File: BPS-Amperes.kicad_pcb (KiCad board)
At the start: 2 copper layers, 40 x 50 mm, 35 parts, among them J1 Conn_02x10_Odd_Even, J2 ShuntConn, J3 PassthroughConn, J4 TestConn, J5 Conn_01x02, U1 INA186A3IDDFT, U2 OPA2196, U4 REF1930AIDDCT

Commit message: Flipped components to the back
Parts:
- C1, C10, C11, C12, C13, C2, C3, C4, C5, C6, C7, C9, D1, D2, FB1, FB2, LOGO0, LOGO1, R1, R2, R3, R4, R5, R6, U1, U2, U4: moved to B.Cu
- moved LOGO1 33.3 mm to (161.5, 111.5), turned to 180 degrees
- moved LOGO0 13.6 mm to (149.9, 80.8), turned to 180 degrees
- moved C13 9.55 mm to (148.0, 91.8), turned to 90 degrees
- moved R6 7.07 mm to (131.5, 81.5), turned to 90 degrees
- moved C11 5.79 mm to (140.1, 95.5)
- moved C12 5.79 mm to (140.1, 98.0)
- moved FB2 5.79 mm to (140.1, 93.0)
- moved C9 5.65 mm to (144.5, 97.5)
- moved C10 5.65 mm to (144.5, 100.0)
- moved FB1 5.65 mm to (144.5, 95.0)
- moved C1 5.18 mm to (140.0, 100.5)
- moved D2 5.03 mm to (131.5, 78.0), turned to -90 degrees
- moved U4 4.98 mm to (144.6, 91.7), turned to -90 degrees
- moved J5 1.13 mm to (139.5, 76.2)
- moved U1 1.08 mm to (145.2, 103.9)
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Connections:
- J5 pad 1: +3V0 -> +1V5
- J5 pad 2: +1V5 -> +3V0

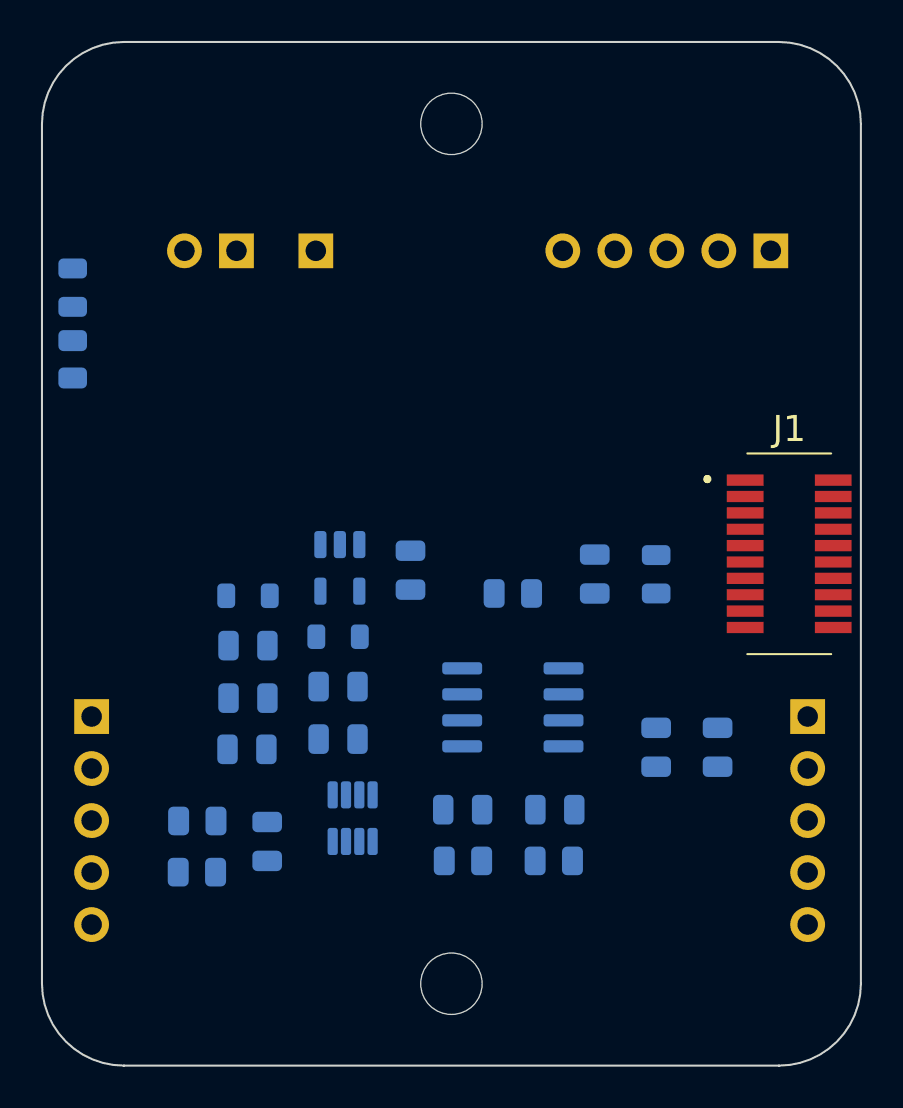
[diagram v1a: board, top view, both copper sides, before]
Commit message: adding ground plane to the back
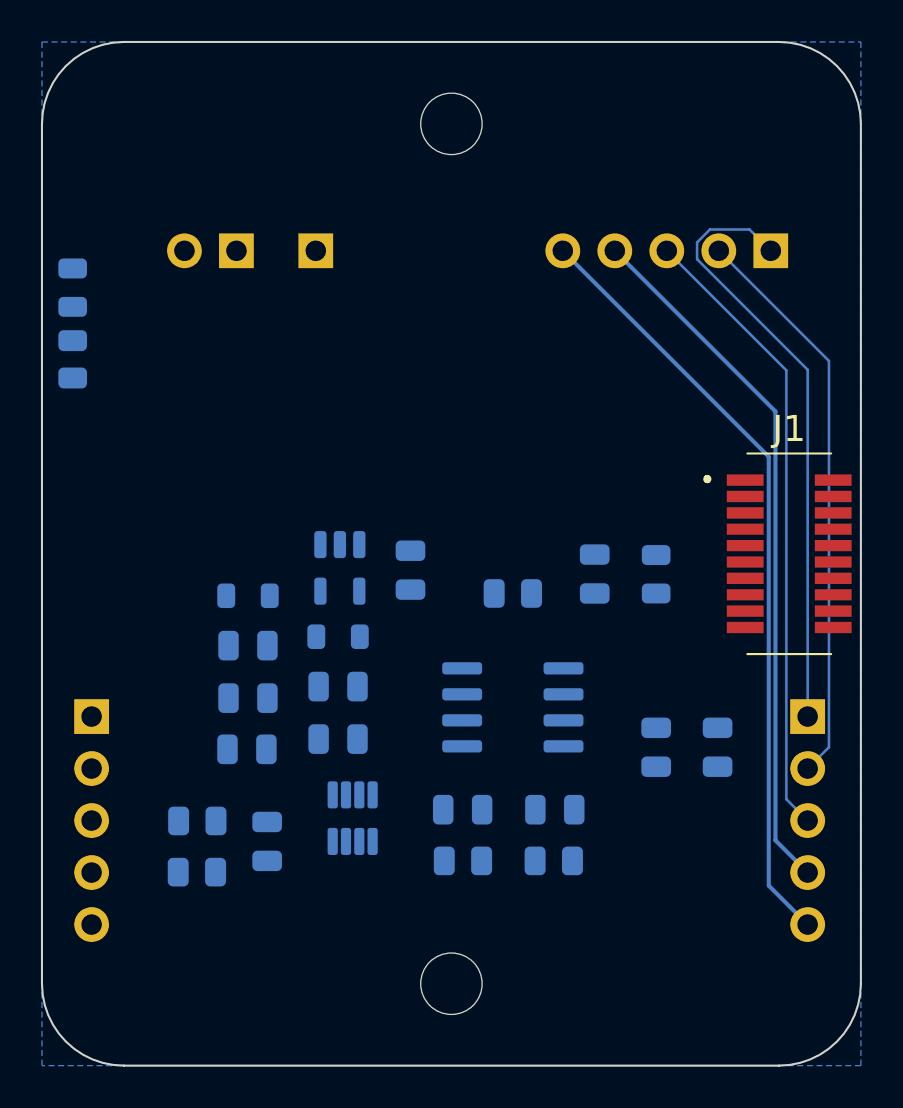
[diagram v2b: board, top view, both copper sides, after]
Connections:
- net Net-(J3-Pin_1) renamed /NOTCON
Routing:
- net /V-: track 0.00 -> 37.9 mm
- net /V+: track 0.00 -> 34.3 mm
- net /TEST: track 0.00 -> 30.7 mm
- net /NOTCON: track 0.00 -> 29.7 mm
- net /SHUNT: track 0.00 -> 27.9 mm
- added copper zone on B.Cu, net GND
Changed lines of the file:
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@@
   (net 32 "Net-(U2B--)")
   (net 33 "unconnected-(U1-NC-Pad6)")
-  (net 34 "Net-(J3-Pin_1)")
+  (net 34 "/NOTCON")
   (net 35 "/SHUNT")
   (net 36 "/TEST")
@@
     (pad "20" smd rect locked (at -3.6 2.15 90) (size 0.55 1.8) (layers "F.Cu" "F.Paste" "F.Mask")
       (net 18 "/Aout") (pinfunction "Pin_20") (pintype "passive"))
-    (model "${KIPRJMOD}/UTSVT-KiCadLibraries/utsvt3d/connectors.3dshapes/53307-2071.stp"
+    (model "${KIPRJMOD}/common/utsvt3d/connectors.3dshapes/53307-2071.stp"
       (offset (xyz 0 0 1.849999996))
       (scale (xyz 1 1 1))
@@
       (stroke (width 0.1) (type solid)) (layer "B.Fab"))
     (pad "1" thru_hole rect (at 0 0 90) (size 1.7 1.7) (drill 1) (layers "*.Cu" "*.Mask")
-      (net 34 "Net-(J3-Pin_1)") (pinfunction "Pin_1") (pintype "passive"))
+      (net 34 "/NOTCON") (pinfunction "Pin_1") (pintype "passive"))
     (pad "2" thru_hole oval (at 0 -2.54 90) (size 1.7 1.7) (drill 1) (layers "*.Cu" "*.Mask")
       (net 35 "/SHUNT") (pinfunction "Pin_2") (pintype "passive"))
@@
       (stroke (width 0.1) (type solid)) (layer "B.Fab"))
     (pad "1" thru_hole rect (at 0 0 180) (size 1.7 1.7) (drill 1) (layers "*.Cu" "*.Mask")
-      (net 34 "Net-(J3-Pin_1)") (pinfunction "Pin_1") (pintype "passive"))
+      (net 34 "/NOTCON") (pinfunction "Pin_1") (pintype "passive"))
     (pad "2" thru_hole oval (at 0 -2.54 180) (size 1.7 1.7) (drill 1) (layers "*.Cu" "*.Mask")
       (net 35 "/SHUNT") (pinfunction "Pin_2") (pintype "passive"))
@@
     (effects (font (size 1 1) (thickness 0.15)) (justify left bottom mirror))
   )
-  (gr_text "V-" (at 165.7 77.5 90) (layer "B.SilkS")
+  (gr_text "V-" (at 155.5 78 90) (layer "B.SilkS")
     (effects (font (size 1 1) (thickness 0.15)) (justify left bottom mirror))
   )
@@
     (effects (font (size 1 1) (thickness 0.15)) (justify left bottom))
   )
-  (gr_text "NC" (at 155.65 77.6 90) (layer "B.SilkS")
+  (gr_text "NC" (at 166.235 78 90) (layer "B.SilkS")
     (effects (font (size 1 1) (thickness 0.15)) (justify left bottom mirror))
   )
@@
     (effects (font (size 1 1) (thickness 0.15) bold) (justify mirror))
   )
-  (gr_text "SHUNT" (at 158.15 77.3 90) (layer "B.SilkS")
+  (gr_text "SHUNT" (at 163.5 78 90) (layer "B.SilkS")
     (effects (font (size 1 1) (thickness 0.15)) (justify left bottom mirror))
   )
@@
     (effects (font (size 1 1) (thickness 0.15) bold) (justify mirror))
   )
-  (gr_text "TEST" (at 160.7 77.3 90) (layer "B.SilkS")
+  (gr_text "TEST" (at 161 78 90) (layer "B.SilkS")
     (effects (font (size 1 1) (thickness 0.15)) (justify left bottom mirror))
   )
@@
     (effects (font (size 1 1) (thickness 0.15) bold) (justify mirror))
   )
-  (gr_text "V+" (at 163.2 77.6 90) (layer "B.SilkS")
+  (gr_text "V+" (at 158.5 78 90) (layer "B.SilkS")
     (effects (font (size 1 1) (thickness 0.15)) (justify left bottom mirror))
   )
@@
     (style (thickness 0.1) (arrow_length 1.27) (text_position_mode 0) (extension_height 0.58642) (extension_offset 0.5) keep_text_aligned)
   )
+  (segment (start 164.5595 75.1595) (end 165.6 76.2) (width 0.127) (layer "B.Cu") (net 34))
+  (segment (start 162 76.61149) (end 162 75.78851) (width 0.127) (layer "B.Cu") (net 34))
+  (segment (start 167.4 98.95) (end 167.4 82.01149) (width 0.127) (layer "B.Cu") (net 34))
+  (segment (start 162 75.78851) (end 162.62901 75.1595) (width 0.127) (layer "B.Cu") (net 34))
+  (segment (start 167.4 82.01149) (end 162 76.61149) (width 0.127) (layer "B.Cu") (net 34))
+  (segment (start 162.62901 75.1595) (end 164.5595 75.1595) (width 0.127) (layer "B.Cu") (net 34))
+  (segment (start 168.4405 100.4495) (end 167.4 101.49) (width 0.127) (layer "B.Cu") (net 35))
+  (segment (start 163.06 76.2) (end 168.4405 81.5805) (width 0.127) (layer "B.Cu") (net 35))
+  (segment (start 168.4405 81.5805) (end 168.4405 100.4495) (width 0.127) (layer "B.Cu") (net 35))
+  (segment (start 167.4 104.03) (end 166.3595 102.9895) (width 0.127) (layer "B.Cu") (net 36))
+  (segment (start 166.3595 102.9895) (end 166.3595 82.0395) (width 0.127) (layer "B.Cu") (net 36))
+  (segment (start 166.3595 82.0395) (end 160.52 76.2) (width 0.127) (layer "B.Cu") (net 36))
+  (segment (start 165.827 84.047) (end 157.98 76.2) (width 0.2) (layer "B.Cu") (net 37))
+  (segment (start 165.827 104.997) (end 165.827 84.047) (width 0.2) (layer "B.Cu") (net 37))
+  (segment (start 167.4 106.57) (end 165.827 104.997) (width 0.2) (layer "B.Cu") (net 37))
+  (segment (start 167.4 109.11) (end 165.5 107.21) (width 0.2) (layer "B.Cu") (net 38))
+  (segment (start 165.5 86.26) (end 155.44 76.2) (width 0.2) (layer "B.Cu") (net 38))
+  (segment (start 165.5 107.21) (end 165.5 86.26) (width 0.2) (layer "B.Cu") (net 38))
+  (zone (net 0) (net_name "") (layer "B.Cu") (hatch edge 0.5)
+    (connect_pads (clearance 0))
+    (min_thickness 0.5) (filled_areas_thickness no)
+    (keepout (tracks allowed) (vias allowed) (pads allowed) (copperpour not_allowed) (footprints allowed))
+    (fill (thermal_gap 0.5) (thermal_bridge_width 0.5))
+    (polygon
+      (pts
+        (xy 150.574997 95.810776)
+        (xy 155.166486 95.823185)
+        (xy 154.980345 101.159241)
+        (xy 150.612225 101.122012)
+      )
+    )
+  )
+  (zone (net 4) (net_name "GND") (layer "B.Cu") (hatch edge 0.5)
+    (connect_pads (clearance 0.5))
+    (min_thickness 0.5) (filled_areas_thickness no)
+    (fill yes (thermal_gap 0.5) (thermal_bridge_width 0.5))
+    (polygon
+      (pts
+        (xy 130 66)
+        (xy 170 66)
+        (xy 170 116)
+        (xy 130 116)
+      )
+    )
+  )
   (group "" (id 9c716276-2a82-4619-908a-de798b1d9a88)

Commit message: Initial tracing with no thoughts
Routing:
- net +3.3V: track 0.00 -> 73.5 mm, vias 0 -> 1
- net +3V0: track 0.00 -> 68.4 mm, vias 0 -> 1
- net GND: track 0.00 -> 49.1 mm, vias 0 -> 1
- net /Aout: track 0.00 -> 41.1 mm, vias 0 -> 2
- net +1V5: track 0.00 -> 34.9 mm, vias 0 -> 1
- net Net-(U2A--): track 0.00 -> 10.8 mm
- net Net-(U2A-+): track 0.00 -> 8.29 mm
- net Net-(U2B--): track 0.00 -> 7.92 mm
- net /RSHH: track 0.00 -> 7.03 mm
- net /RSHL: track 0.00 -> 6.34 mm
- net Net-(J2-Pin_2): track 0.00 -> 5.31 mm
- net /NOTCON: track 29.7 -> 24.5 mm
- net Net-(C3-Pad1): track 0.00 -> 5.12 mm
- net Net-(U4-VBIAS): track 0.00 -> 4.99 mm
- net Net-(U1-OUT): track 0.00 -> 3.89 mm
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
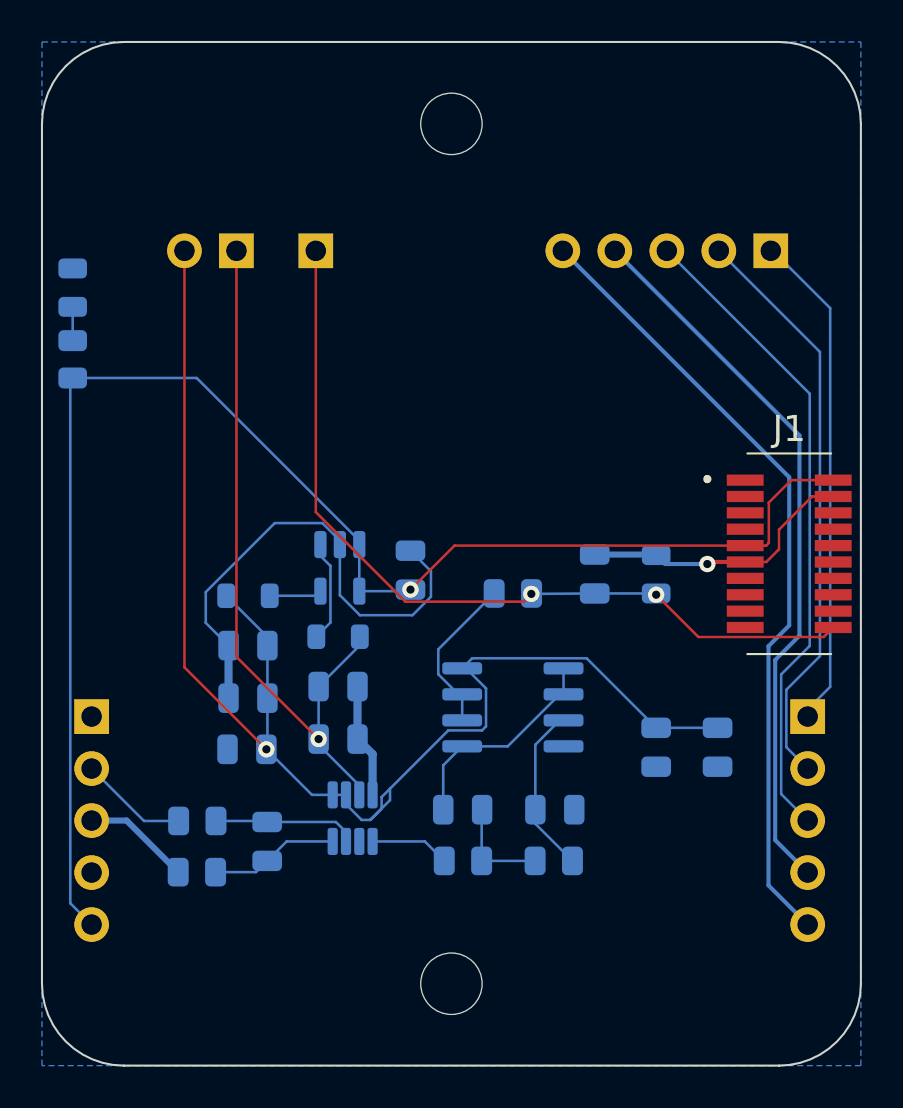
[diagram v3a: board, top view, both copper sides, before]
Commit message: Updated component blocking
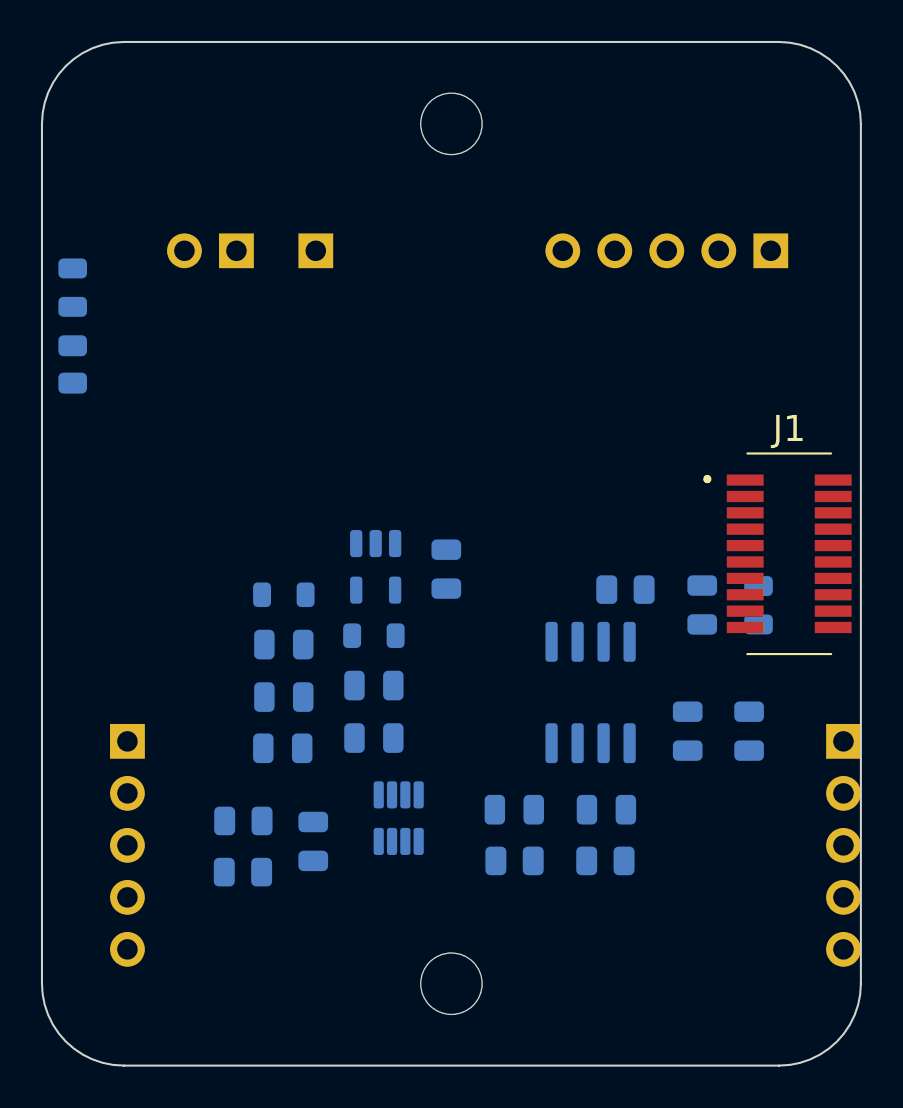
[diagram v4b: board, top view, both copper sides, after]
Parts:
- moved R5 5.50 mm to (158.5, 92.8)
- moved C6 5.46 mm to (162.2, 93.5)
- moved D1 5.22 mm to (165.0, 93.5)
- moved U2 3.87 mm to (156.8, 97.8), turned to 90 degrees
- moved R3 2.52 mm to (153.1, 106.0)
- moved R4 2.52 mm to (157.5, 106.0)
- moved C3 2.52 mm to (153.1, 103.5)
- moved C4 2.52 mm to (157.6, 103.5), turned to 180 degrees
- moved C2 2.25 mm to (143.2, 105.0)
- moved R1 2.25 mm to (139.8, 104.0)
- moved R2 2.25 mm to (139.8, 106.5)
- moved U1 2.25 mm to (147.4, 103.9)
- moved J2 2.13 mm to (134.2, 100.2)
- moved J3 2.13 mm to (169.2, 100.2)
- moved C1 1.75 mm to (141.8, 100.5)
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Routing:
- net +3.3V: track 73.5 -> 0.00 mm, vias 1 -> 0
- net +3V0: track 68.4 -> 0.00 mm, vias 1 -> 0
- net GND: track 49.1 -> 0.00 mm, vias 1 -> 0
- net /Aout: track 41.1 -> 0.00 mm, vias 2 -> 0
- net /V-: track 38.7 -> 0.00 mm
- net /V+: track 35.3 -> 0.00 mm
- net +1V5: track 34.9 -> 0.00 mm, vias 1 -> 0
- net /TEST: track 31.8 -> 0.00 mm
- net /SHUNT: track 28.4 -> 0.00 mm
- net /NOTCON: track 24.5 -> 0.00 mm
- net Net-(U2A--): track 10.8 -> 0.00 mm
- net Net-(U2A-+): track 8.29 -> 0.00 mm
- net Net-(U2B--): track 7.92 -> 0.00 mm
- net /RSHH: track 7.03 -> 0.00 mm
- net /RSHL: track 6.34 -> 0.00 mm
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- removed copper zone on B.Cu, net GND

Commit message: Fixed 3.3V Zener & Read Me
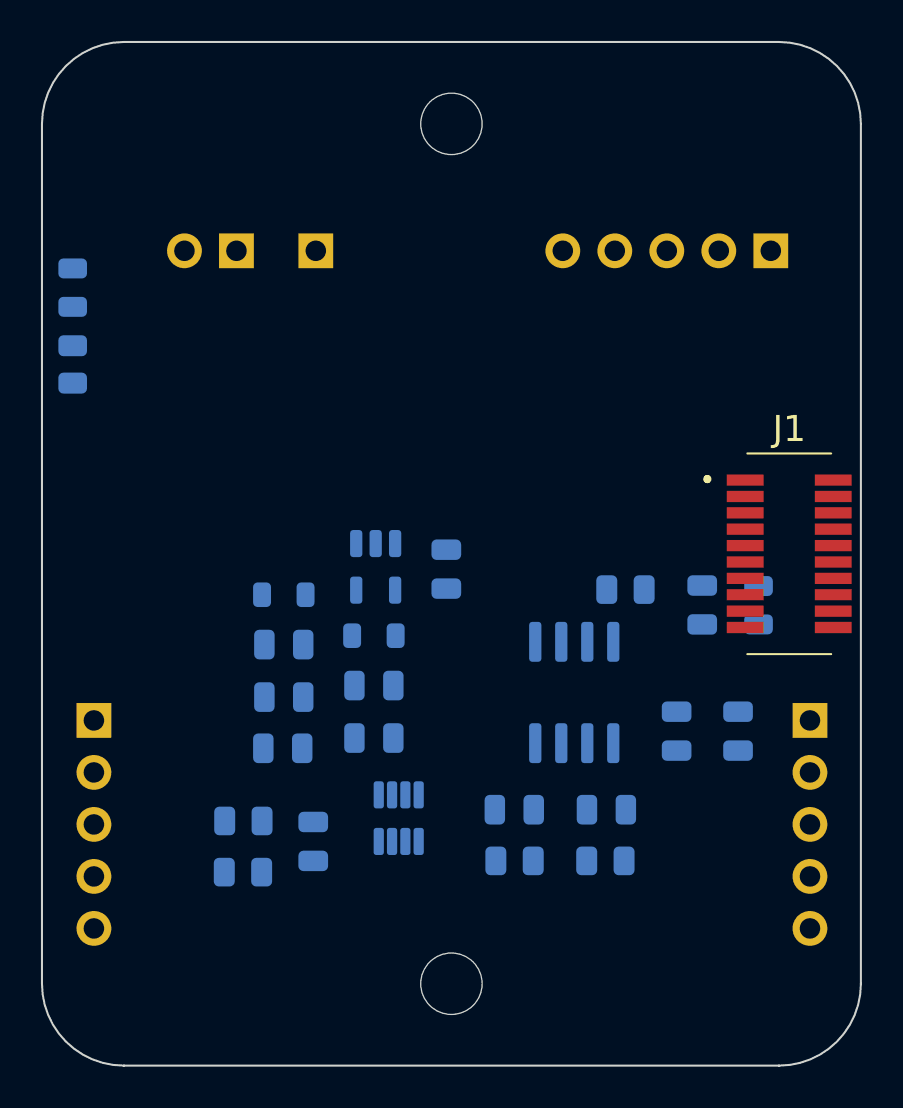
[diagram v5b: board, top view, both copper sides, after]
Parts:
- moved J2 1.93 mm to (132.5, 99.1)
- moved J3 1.93 mm to (167.5, 99.1)
- moved U2 0.80 mm to (156.0, 97.8)
- moved C5 0.54 mm to (164.0, 99.7)
- moved C7 0.54 mm to (161.0, 99.7)
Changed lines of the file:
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@@
   )
   (footprint "Capacitor_SMD:C_0805_2012Metric" (layer "B.Cu")
-    (at 164.54 99.6625 -90)
+    (at 164 99.6625 -90)
     (descr "Capacitor SMD 0805 (2012 Metric), square (rectangular) end terminal, IPC_7351 nominal, (Body size source: IPC-SM-782 page 76, https://www.pcb-3d.com/wordpress/wp-content/uploads/ipc-sm-782a_amendment_1_and_2.pdf, https://docs.google.com/spreadsheets/d/1BsfQQcO9C6DZCsRaXUlFlo91Tg2WpOkGARC1WS5S8t0/edit?usp=sharing), generated with kicad-footprint-generator")
     (tags "capacitor")
@@
   )
   (footprint "Connector_PinSocket_2.54mm:PinSocket_1x05_P2.54mm_Vertical" (layer "B.Cu")
-    (at 134.175 100.1625 180)
+    (at 132.537179 99.138763 180)
     (descr "Through hole straight socket strip, 1x05, 2.54mm pitch, single row (from Kicad 4.0.7), script generated")
     (tags "Through hole socket strip THT 1x05 2.54mm single row")
@@
   )
   (footprint "Capacitor_SMD:C_0805_2012Metric" (layer "B.Cu")
-    (at 161.54 99.6625 -90)
+    (at 161 99.6625 -90)
     (descr "Capacitor SMD 0805 (2012 Metric), square (rectangular) end terminal, IPC_7351 nominal, (Body size source: IPC-SM-782 page 76, https://www.pcb-3d.com/wordpress/wp-content/uploads/ipc-sm-782a_amendment_1_and_2.pdf, https://docs.google.com/spreadsheets/d/1BsfQQcO9C6DZCsRaXUlFlo91Tg2WpOkGARC1WS5S8t0/edit?usp=sharing), generated with kicad-footprint-generator")
     (tags "capacitor")
@@
   )
   (footprint "Package_SO:SOIC-8_3.9x4.9mm_P1.27mm" (layer "B.Cu")
-    (at 156.7975 97.775 90)
+    (at 156 97.775 90)
     (descr "SOIC, 8 Pin (JEDEC MS-012AA, https://www.analog.com/media/en/package-pcb-resources/package/pkg_pdf/soic_narrow-r/r_8.pdf), generated with kicad-footprint-generator ipc_gullwing_generator.py")
     (tags "SOIC SO")
@@
   )
   (footprint "Connector_PinSocket_2.54mm:PinSocket_1x05_P2.54mm_Vertical" (layer "B.Cu")
-    (at 169.15 100.1625 180)
+    (at 167.512179 99.138763 180)
     (descr "Through hole straight socket strip, 1x05, 2.54mm pitch, single row (from Kicad 4.0.7), script generated")
     (tags "Through hole socket strip THT 1x05 2.54mm single row")
@@
   )
   (dimension (type orthogonal) (layer "Dwgs.User")
-    (pts (xy 134.175 100.1625) (xy 169.1502 100.2107))
+    (pts (xy 132.537179 99.138763) (xy 167.512379 99.186963))
     (height -13.0328)
     (orientation 0)
-    (gr_text "34.9752 mm" (at 151.6626 85.9797) (layer "Dwgs.User")
+    (gr_text "34.9752 mm" (at 150.024779 84.955963) (layer "Dwgs.User")
       (effects (font (size 1 1) (thickness 0.15)))
     )
